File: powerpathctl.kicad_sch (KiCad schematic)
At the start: 9 parts, among them J10 Conn_01x06_Male, J11 Conn_01x06_Male_BAT_data, J8 Conn_01x03_Male_BAT_PWR_IN_NU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, J9 Conn_01x03_Male_BAT_PWR, Q1 SI7149ADP-T1-GE3, U7 LTC4412ES6

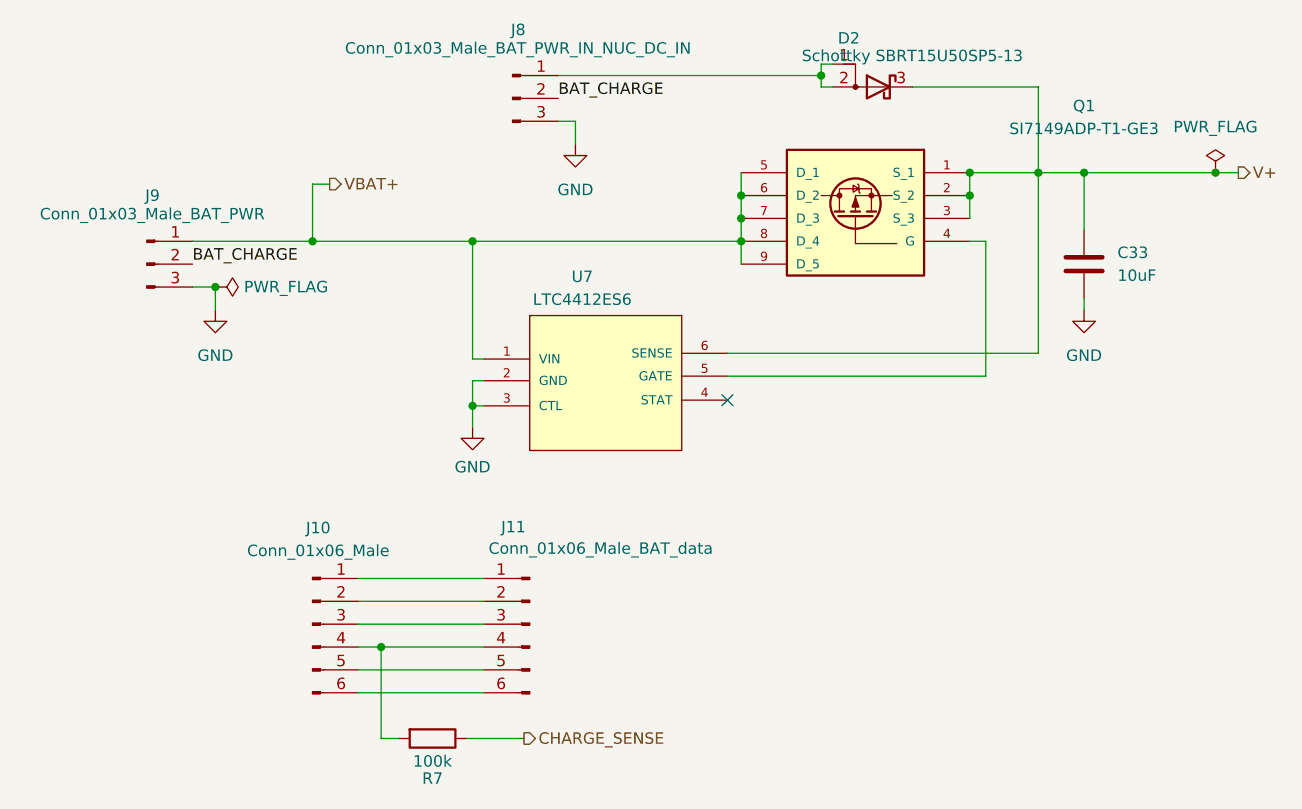
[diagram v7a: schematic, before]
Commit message: Voltage divider added to powerpath controller
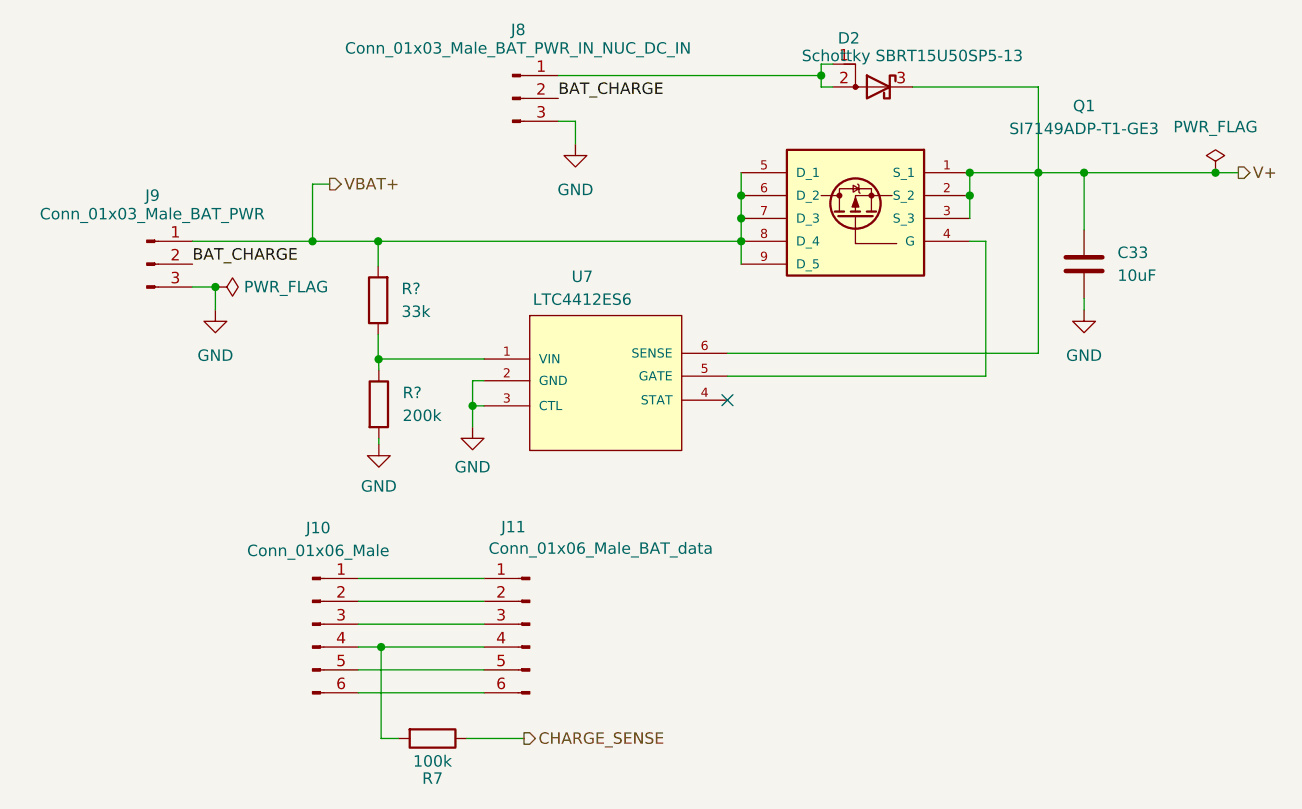
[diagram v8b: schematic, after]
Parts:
- added R?: 33k, symbol Device:R
- added R?: 200k, symbol Device:R
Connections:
- net GND: now also R?.2
- net VBAT+: now also R?.2; no longer U7.1 (VIN)
- new net: R?.1, U7.1 (VIN)
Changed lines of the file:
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@@
   (junction (at 203.835 67.31) (diameter 0) (color 0 0 0 0)
   )
-  (junction (at 121.285 74.93) (diameter 0) (color 0 0 0 0)
+  (junction (at 110.7948 74.93) (diameter 0) (color 0 0 0 0)
   )
   (junction (at 151.13 74.93) (diameter 0) (color 0 0 0 0)
@@
   )
   (junction (at 151.13 72.39) (diameter 0) (color 0 0 0 0)
+  )
+  (junction (at 110.8456 88.0364) (diameter 0) (color 0 0 0 0)
   )
   (junction (at 184.15 67.31) (diameter 0) (color 0 0 0 0)
@@
     (stroke (width 0) (type default) (color 0 0 0 0))
   )
+  (wire (pts (xy 110.7948 74.93) (xy 151.13 74.93))
+    (stroke (width 0) (type default) (color 0 0 0 0))
+  )
   (wire (pts (xy 176.53 67.31) (xy 184.15 67.31))
     (stroke (width 0) (type default) (color 0 0 0 0))
@@
     (stroke (width 0) (type default) (color 0 0 0 0))
   )
+  (wire (pts (xy 110.871 96.8502) (xy 110.871 97.4852))
+    (stroke (width 0) (type default) (color 0 0 0 0))
+  )
   (wire (pts (xy 160.02 57.785) (xy 161.29 57.785))
     (stroke (width 0) (type default) (color 0 0 0 0))
@@
     (stroke (width 0) (type default) (color 0 0 0 0))
   )
+  (wire (pts (xy 110.871 89.2302) (xy 110.8456 88.0364))
+    (stroke (width 0) (type default) (color 0 0 0 0))
+  )
   (wire (pts (xy 111.125 130.175) (xy 113.03 130.175))
     (stroke (width 0) (type default) (color 0 0 0 0))
@@
     (stroke (width 0) (type default) (color 0 0 0 0))
   )
-  (wire (pts (xy 121.285 74.93) (xy 151.13 74.93))
+  (wire (pts (xy 103.505 74.93) (xy 110.7948 74.93))
     (stroke (width 0) (type default) (color 0 0 0 0))
   )
@@
     (stroke (width 0) (type default) (color 0 0 0 0))
   )
+  (wire (pts (xy 110.7948 74.93) (xy 110.7948 77.6732))
+    (stroke (width 0) (type default) (color 0 0 0 0))
+  )
   (wire (pts (xy 105.41 68.58) (xy 103.505 68.58))
     (stroke (width 0) (type default) (color 0 0 0 0))
@@
     (stroke (width 0) (type default) (color 0 0 0 0))
   )
-  (wire (pts (xy 103.505 74.93) (xy 121.285 74.93))
+  (wire (pts (xy 110.7948 85.2932) (xy 110.7948 88.011))
     (stroke (width 0) (type default) (color 0 0 0 0))
   )
@@
     (stroke (width 0) (type default) (color 0 0 0 0))
   )
-  (wire (pts (xy 121.285 88.011) (xy 122.555 88.011))
-    (stroke (width 0) (type default) (color 0 0 0 0))
-  )
-  (wire (pts (xy 121.285 74.93) (xy 121.285 88.011))
+  (wire (pts (xy 110.7948 88.011) (xy 122.555 88.011))
     (stroke (width 0) (type default) (color 0 0 0 0))
   )
@@
     (pin "3")
   )
+  (symbol (lib_id "Device:R") (at 110.7948 81.4832 180) (unit 1)
+    (in_bom yes) (on_board yes) (fields_autoplaced)
+    (property "Reference" "R?" (id 0) (at 113.3856 80.2131 0)
+      (effects (font (size 1.27 1.27)) (justify right))
+    )
+    (property "Value" "33k" (id 1) (at 113.3856 82.7531 0)
+      (effects (font (size 1.27 1.27)) (justify right))
+    )
+    (property "Footprint" "" (id 2) (at 112.5728 81.4832 90))
+    (property "Datasheet" "~" (id 3) (at 110.7948 81.4832 0)
+      (effects (font (size 1.27 1.27)) hide)
+    )
+    (pin "1")
+    (pin "2")
+  )
   (symbol (lib_id "Connector:Conn_01x03_Male") (at 85.09 77.47 0) (unit 1)
     (in_bom yes) (on_board yes)
@@
     (pin "1")
     (pin "2")
+  )
+  (symbol (lib_id "power:GND") (at 110.871 97.4852 0) (unit 1)
+    (in_bom yes) (on_board yes) (fields_autoplaced)
+    (property "Reference" "#PWR?" (id 0) (at 110.871 103.8352 0)
+      (effects (font (size 1.27 1.27)) hide)
+    )
+    (property "Value" "GND" (id 1) (at 110.871 102.1588 0))
+    (property "Footprint" "" (id 2) (at 110.871 97.4852 0)
+      (effects (font (size 1.27 1.27)) hide)
+    )
+    (property "Datasheet" "" (id 3) (at 110.871 97.4852 0)
+      (effects (font (size 1.27 1.27)) hide)
+    )
+    (pin "1")
   )
   (symbol (lib_id "Device:C") (at 189.23 77.47 0) (unit 1)
@@
     (pin "9")
   )
+  (symbol (lib_id "Device:R") (at 110.871 93.0402 0) (unit 1)
+    (in_bom yes) (on_board yes) (fields_autoplaced)
+    (property "Reference" "R?" (id 0) (at 113.5126 91.7701 0)
+      (effects (font (size 1.27 1.27)) (justify left))
+    )
+    (property "Value" "200k" (id 1) (at 113.5126 94.3101 0)
+      (effects (font (size 1.27 1.27)) (justify left))
+    )
+    (property "Footprint" "" (id 2) (at 109.093 93.0402 90))
+    (property "Datasheet" "~" (id 3) (at 110.871 93.0402 0)
+      (effects (font (size 1.27 1.27)) hide)
+    )
+    (pin "1")
+    (pin "2")
+  )
   (symbol (lib_id "power:GND") (at 189.23 82.55 0) (unit 1)
